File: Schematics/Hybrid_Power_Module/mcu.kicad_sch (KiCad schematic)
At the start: 42 parts, among them J5 USB_C_Female_USB2_Small, J6 SWD_B, J7 Stack Male Edge Connector, SW1 SW_STM_RESET, SW2 SW_STM_BOOT_MODE, U13 CP2102N-A02-GQFN20R, U14 STM32F103CBT6, U15 ISO1044BDR, U16 W25Q128JVS, Y1 X322516MMB4SI

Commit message: fix part number and bom formation, update mostfet based on stock
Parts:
- C33, C35: JLCPCB C32949 -> (none); LCSC (none) -> C32949
- C34, C46, C47, C48: JLCPCB C14663 -> (none); LCSC (none) -> C14663
- C36, C44, C45: JLCPCB C15849 -> (none); LCSC (none) -> C15849
- C38, C39, C41, C42: JLCPCB C1525 -> (none); LCSC (none) -> C1525
- C40: JLCPCB C96446 -> (none); LCSC (none) -> C96446
- C43: JLCPCB C57112 -> (none); LCSC (none) -> C57112
- D8: JLCPCB C72038 -> (none); LCSC (none) -> C72038
- FB1: JLCPCB C1002 -> (none); LCSC (none) -> C1002
- J5: JLCPCB C5178541 -> (none); LCSC (none) -> C5178541
- R20, R21, R24: JLCPCB C25803 -> (none); LCSC (none) -> C25803
- R22, R23: JLCPCB C23186 -> (none); LCSC (none) -> C23186
- R25: JLCPCB C31850 -> (none); LCSC (none) -> C31850
- R26: JLCPCB C25819 -> (none); LCSC (none) -> C25819
- R27: JLCPCB C21190 -> (none); LCSC (none) -> C21190
- R28: JLCPCB C23228 -> (none); LCSC (none) -> C23228
- R29, R30: JLCPCB C25804 -> (none); LCSC (none) -> C25804
- SW1, SW2: JLCPCB C318884 -> (none); LCSC (none) -> C318884
- U13: JLCPCB C969913 -> (none); LCSC (none) -> C969913
- U14: JLCPCB C8304 -> (none); LCSC (none) -> C8304
- U15: JLCPCB C2878225 -> (none); LCSC (none) -> C2878225
- U16: JLCPCB C97521 -> (none); LCSC (none) -> C97521
- Y1: JLCPCB C13738 -> (none); LCSC (none) -> C13738
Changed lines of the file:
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@@
 			)
 		)
-		(property "JLCPCB" "C23186"
+		(property "LCSC" "C23186"
 			(at 43.18 166.37 0)
 			(effects
@@
 			)
 		)
-		(property "LCSC" ""
-			(at 266.7 128.27 0)
-			(effects
-				(font
-					(size 1.27 1.27)
-				)
-				(hide yes)
-			)
-		)
-		(property "JLCPCB" "C14663"
+		(property "LCSC" "C14663"
 			(at 266.7 128.27 0)
 			(effects
@@
 			)
 		)
-		(property "JLCPCB" "C318884"
+		(property "LCSC" "C318884"
 			(at 24.13 99.06 0)
 			(effects
@@
 			)
 		)
-		(property "JLCPCB" "C969913"
+		(property "LCSC" "C969913"
 			(at 99.06 160.02 0)
 			(effects
@@
 			)
 		)
-		(property "JLCPCB" "C21190"
+		(property "LCSC" "C21190"
 			(at 85.09 133.35 0)
 			(effects
@@
 			)
 		)
-		(property "JLCPCB" "C97521"
+		(property "LCSC" "C97521"
 			(at 262.89 90.17 0)
 			(effects
@@
 			)
 		)
-		(property "JLCPCB" "C1002"
-			(at 157.48 22.86 90)
+		(property "LCSC" "C1002"
+			(at 157.48 22.86 0)
 			(effects
 				(font
@@
 			)
 		)
-		(property "JLCPCB" "C14663"
+		(property "LCSC" "C14663"
 			(at 33.02 102.87 0)
 			(effects
@@
 			)
 		)
-		(property "JLCPCB" "C15849"
+		(property "LCSC" "C15849"
 			(at 78.74 153.67 0)
 			(effects
@@
 			)
 		)
-		(property "JLCPCB" "C13738"
+		(property "LCSC" "C13738"
 			(at 38.1 25.4 0)
 			(effects
@@
 			)
 		)
-		(property "JLCPCB" "C1525"
+		(property "LCSC" "C1525"
 			(at 113.03 26.67 0)
 			(effects
@@
 			)
 		)
-		(property "JLCPCB" "C318884"
+		(property "LCSC" "C318884"
 			(at 31.75 64.77 0)
 			(effects
@@
 			)
 		)
-		(property "JLCPCB" "C14663"
-			(at 271.78 76.2 90)
+		(property "LCSC" "C14663"
+			(at 271.78 76.2 0)
 			(effects
 				(font
@@
 			)
 		)
-		(property "JLCPCB" "C8304"
+		(property "LCSC" "C8304"
 			(at 128.27 72.39 0)
 			(effects
@@
 			)
 		)
-		(property "JLCPCB" "C1525"
+		(property "LCSC" "C1525"
 			(at 92.71 26.67 0)
 			(effects
@@
 			)
 		)
-		(property "JLCPCB" "C1525"
+		(property "LCSC" "C1525"
 			(at 102.87 26.67 0)
 			(effects
@@
 			)
 		)
-		(property "JLCPCB" "C23186"
+		(property "LCSC" "C23186"
 			(at 43.18 163.83 0)
 			(effects
@@
 			)
 		)
-		(property "JLCPCB" "C32949"
+		(property "LCSC" "C32949"
 			(at 30.48 29.21 0)
 			(effects
@@
 			)
 		)
-		(property "JLCPCB" "C5178541"
+		(property "LCSC" "C5178541"
 			(at 22.86 176.53 0)
 			(effects
@@
 			)
 		)
-		(property "JLCPCB" "C25803"
-			(at 67.31 63.5 90)
+		(property "LCSC" "C25803"
+			(at 67.31 63.5 0)
 			(effects
 				(font
@@
 			)
 		)
-		(property "JLCPCB" "C15849"
+		(property "LCSC" "C15849"
 			(at 165.1 26.67 0)
 			(effects
@@
 			)
 		)
-		(property "JLCPCB" "C96446"
+		(property "LCSC" "C96446"
 			(at 102.87 127 0)
 			(effects
@@
 			)
 		)
-		(property "JLCPCB" "C72038"
+		(property "LCSC" "C72038"
 			(at 178.435 85.09 0)
 			(effects
@@
 			)
 		)
-		(property "JLCPCB" "C25803"
+		(property "LCSC" "C25803"
 			(at 26.67 68.58 0)
 			(effects
@@
 			)
 		)
-		(property "JLCPCB" "C25804"
+		(property "LCSC" "C25804"
 			(at 226.06 88.9 0)
 			(effects
@@
 			)
 		)
-		(property "JLCPCB" "C23228"
+		(property "LCSC" "C23228"
 			(at 167.005 85.09 0)
 			(effects
@@
 			)
 		)
-		(property "JLCPCB" "C1525"
+		(property "LCSC" "C1525"
 			(at 123.19 26.67 0)
 			(effects
@@
 			)
 		)
-		(property "JLCPCB" "C25804"
+		(property "LCSC" "C25804"
 			(at 233.68 88.9 0)
 			(effects
@@
 			)
 		)
-		(property "JLCPCB" "C31850"
+		(property "LCSC" "C31850"
 			(at 68.58 146.05 0)
 			(effects
@@
 			)
 		)
-		(property "LCSC" ""
-			(at 256.54 134.62 0)
-			(effects
-				(font
-					(size 1.27 1.27)
-				)
-				(hide yes)
-			)
-		)
-		(property "JLCPCB" "C2878225"
+		(property "LCSC" "C2878225"
 			(at 256.54 134.62 0)
 			(effects
@@
 			)
 		)
-		(property "LCSC" ""
-			(at 246.38 128.27 0)
-			(effects
-				(font
-					(size 1.27 1.27)
-				)
-				(hide yes)
-			)
-		)
-		(property "JLCPCB" "C14663"
+		(property "LCSC" "C14663"
 			(at 246.38 128.27 0)
 			(effects
@@
 			)
 		)
-		(property "JLCPCB" "C25803"
+		(property "LCSC" "C25803"
 			(at 33.02 95.25 0)
 			(effects
@@
 			)
 		)
-		(property "JLCPCB" "C57112"
+		(property "LCSC" "C57112"
 			(at 139.7 26.67 0)
 			(effects
@@
 			)
 		)
-		(property "JLCPCB" "C25819 "
+		(property "LCSC" "C25819 "
 			(at 68.58 153.67 0)
 			(effects
@@
 			)
 		)
-		(property "JLCPCB" "C32949"
+		(property "LCSC" "C32949"
 			(at 45.72 29.21 0)
 			(effects
@@
 			)
 		)
-		(property "JLCPCB" "C15849"
+		(property "LCSC" "C15849"
 			(at 148.59 26.67 0)
 			(effects

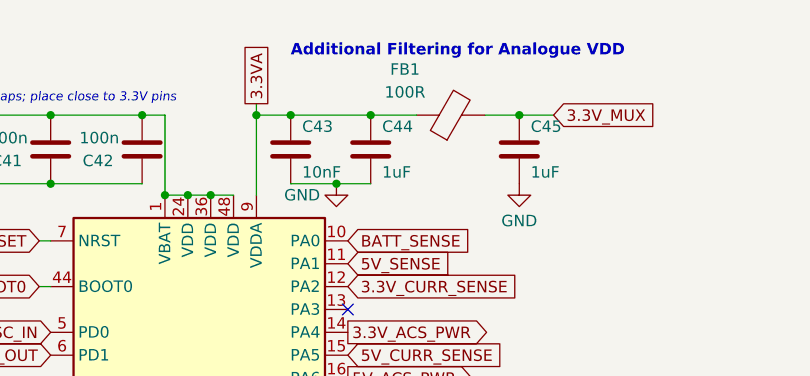
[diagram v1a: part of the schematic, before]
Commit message: minor updates to part numbers and silkscreen
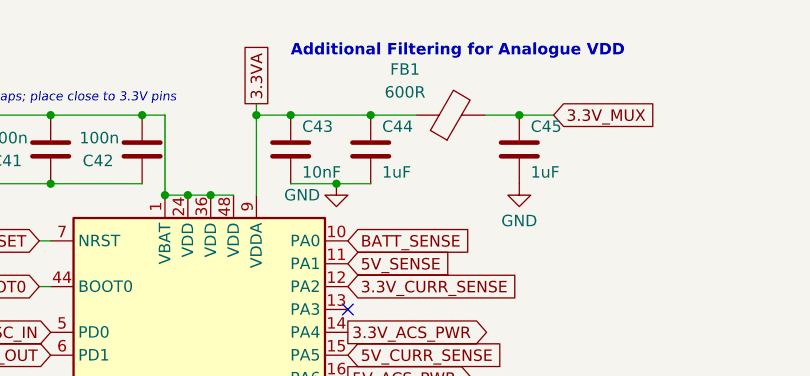
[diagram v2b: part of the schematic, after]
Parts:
- D8: LCSC C72038 -> C2290
- FB1: value 100R -> 600R
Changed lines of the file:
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@@
 			)
 		)
-		(property "Value" "100R"
+		(property "Value" "600R"
 			(at 152.4 20.32 90)
 			(effects
@@
 			)
 		)
-		(property "LCSC" "C72038"
+		(property "LCSC" "C2290"
 			(at 178.435 85.09 0)
 			(effects

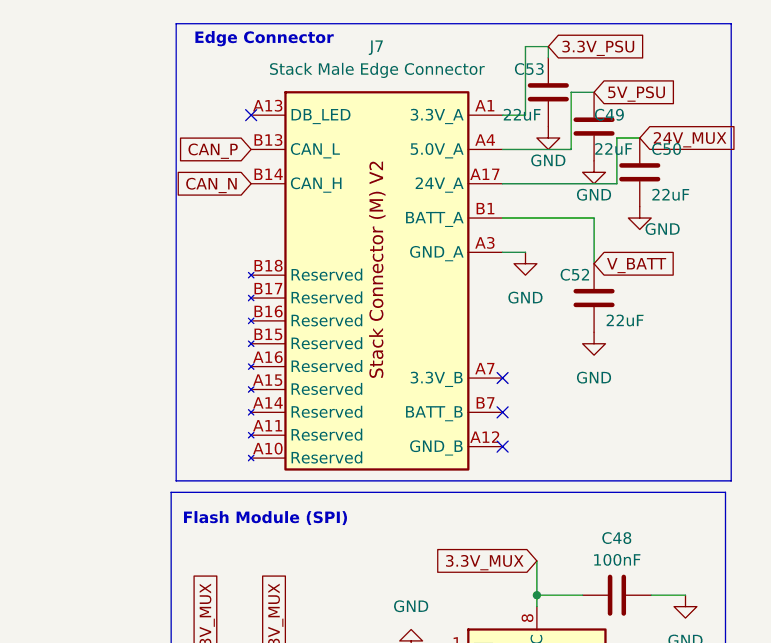
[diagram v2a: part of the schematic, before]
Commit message: changed current sense and switched to bidirectional TVS for GSE power
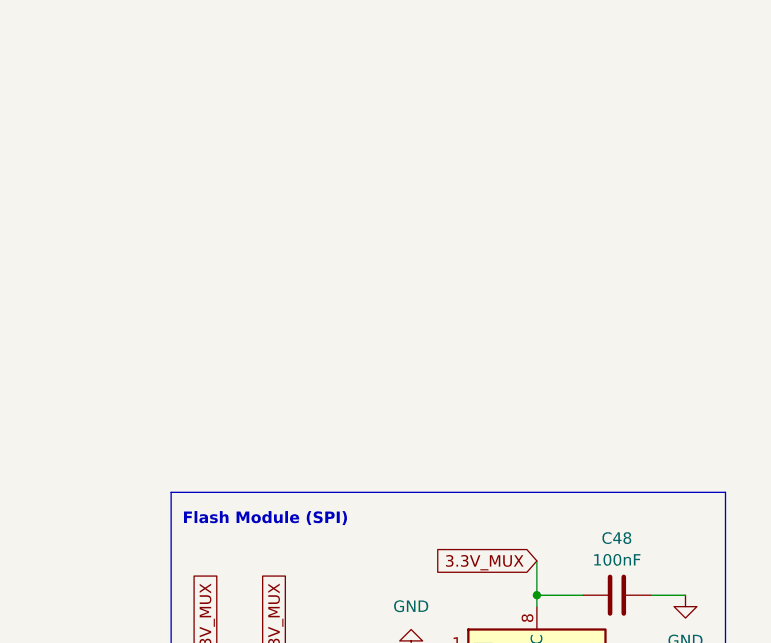
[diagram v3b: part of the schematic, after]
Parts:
- removed C49, C50, C52, C53: 22uF, Capacitor_SMD:C_1206_3216Metric, symbol Device:C
- removed J7: Stack Male Edge Connector, Connector_PCBEdge:BUS_PCIexpress_x1, symbol EdgeConnectorV2:Stack Male Edge Connector
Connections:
- net 5.0V_A renamed 5V_PSU
- no-connect marks 31 -> 27
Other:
- note removed: "Edge Connector"

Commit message: final board submitted to cart
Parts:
- removed C47: 100nF, Capacitor_SMD:C_0603_1608Metric, symbol Device:C
- removed U15: ISO1044BDR, ISO1044:SOIC_1044BDR_TEX, symbol Interface_CAN_LIN:ISO1044BD
- added U15: TCAN1051HGVDR, ISO1044:SOIC_1044BDR_TEX, symbol Interface_CAN_LIN:TCAN330
- U16: value W25Q128JVS -> BY25Q128ES; Digikey (none) -> 5369-BY25Q128ESSIG(R)CT-ND; LCSC C97521 -> (none)
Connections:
- net 3.3V_MUX: no longer C46.1
- net 5V_PSU: now also C46.2, U15.3 (VCC)
- net CAN_N: now also U15.6 (CANL)
- net CAN_P: now also U15.7 (CANH)
- net CAN_RX: now also U15.4 (RXD)
- net CAN_TX: now also U15.1 (TXD)
- net GND: now also C46.1, U15.2 (GND); no longer C46.2
- no-connect marks 27 -> 29
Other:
- note added: "NOTE: Not typtical CANT used, ISO1044BDR was out of stock"
- note added: "NOTE: Not typtical flash used, pins are identical but lower write speeds"
